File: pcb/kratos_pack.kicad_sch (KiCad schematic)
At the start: 97 parts, among them J1 USB_C_Receptacle_USB2.0, J2 PROG_CONN, J3 DBG_UART, J4 BAT_MID+NTC, J5 BAT_7.4V, J6 BAT_0V, J7 OUT+, J8 OUT-, Q1 AON7403, Q2 AON7414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

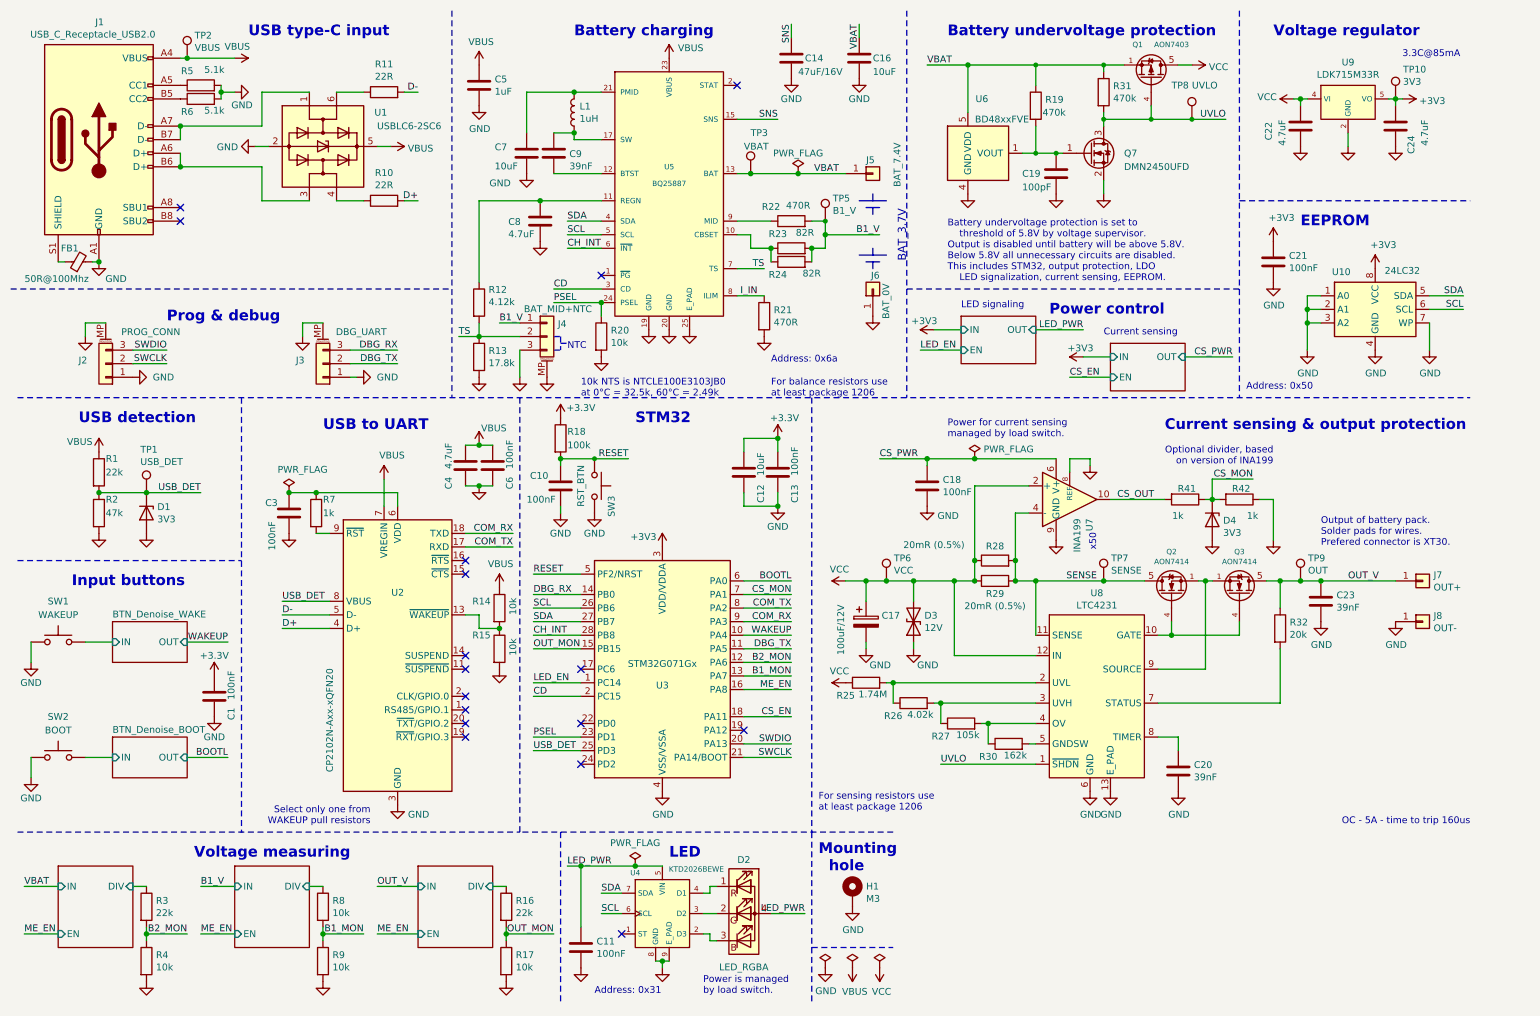
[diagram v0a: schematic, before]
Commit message: Schema & PCB: Fix USB detection by MCU and USB converter, hide GND labels
USB detection circuit is now connected only to MCU.
Converter from USB to UART (CP2102) is directly connected to VBUS.
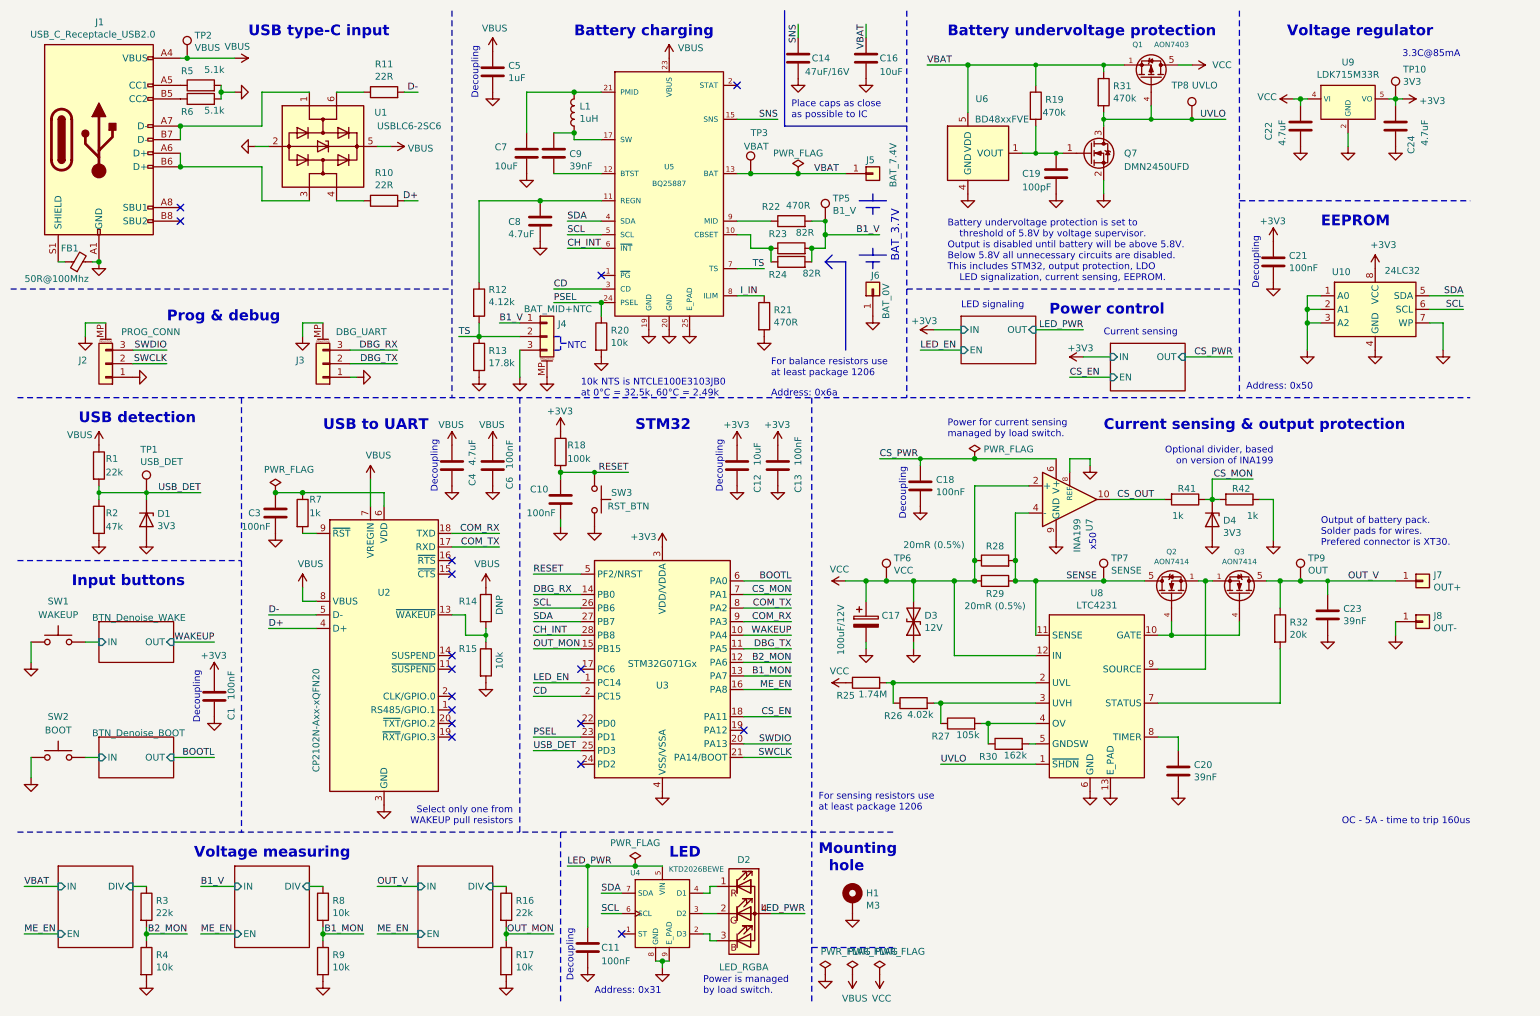
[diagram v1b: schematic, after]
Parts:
- R14: value 10k -> DNP
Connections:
- net USB_DET: no longer U2.8 (VBUS)
- net VBUS: now also U2.8 (VBUS)
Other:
- note added: "Decoupling"
- note added: "Place caps as close as possible to IC"
- moved on the sheet: C10, C11, C12, C13, C14, C16, C18, C23, C3, C4, C5, D1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

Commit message: Schema: Removed intended ILIM connection, mirror connectors, fix typos
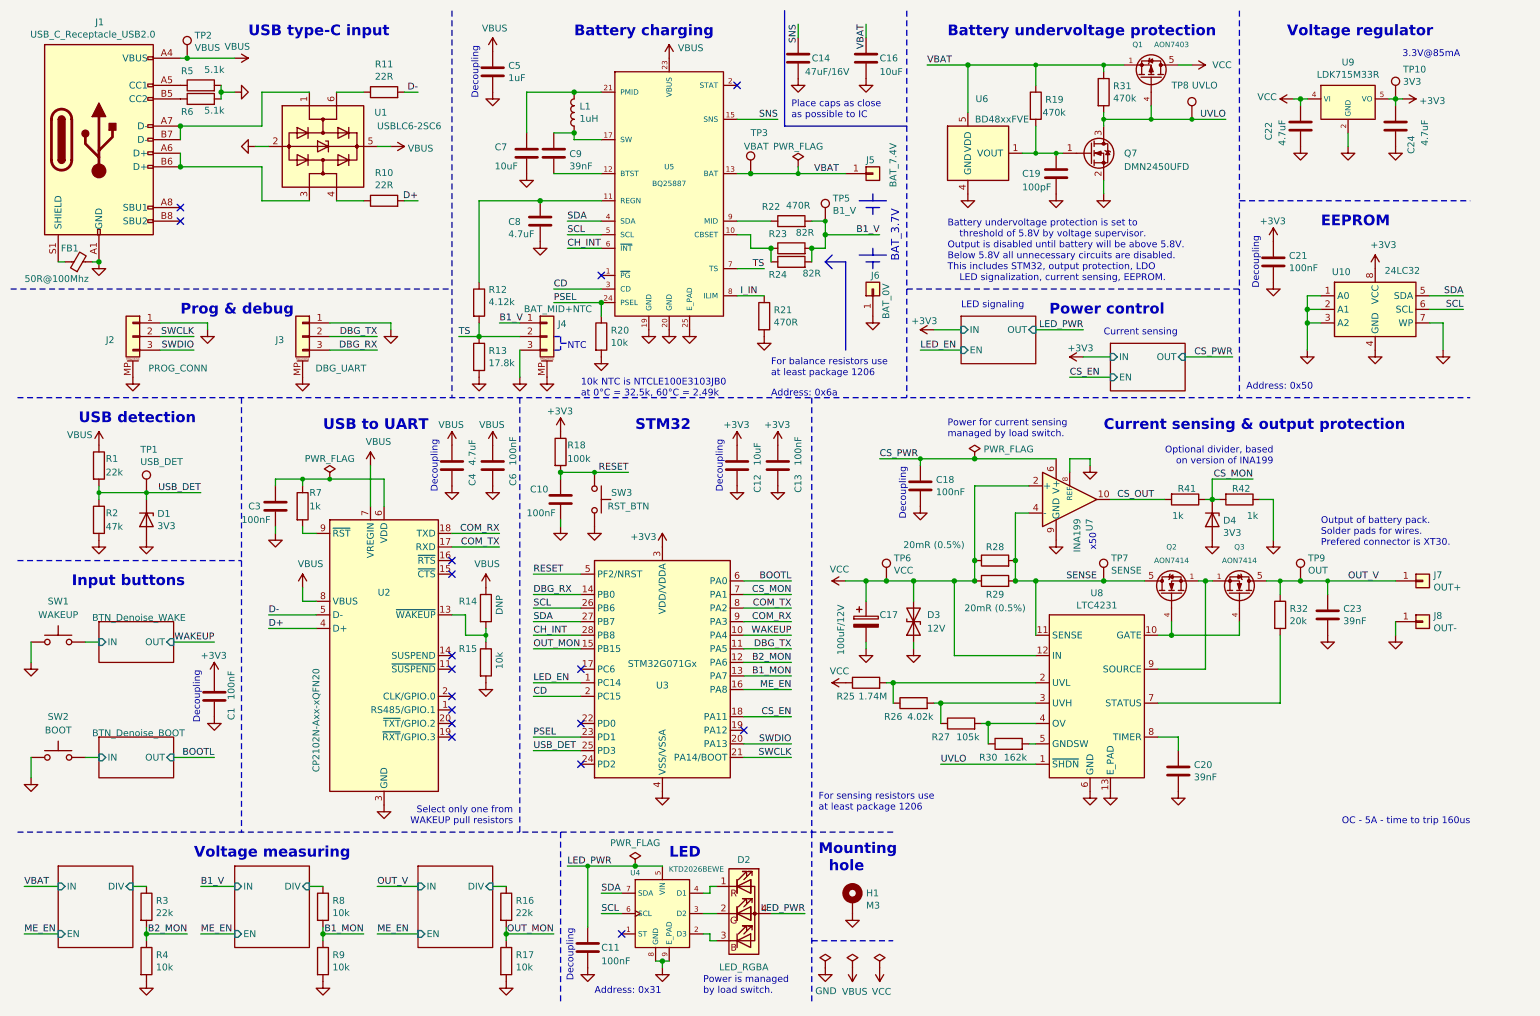
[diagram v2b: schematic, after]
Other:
- note added: "10k NTC is NTCLE100E3103JB0 at 0°C = 32.5k, 60°C = 2.49k"
- note added: "3.3V@85mA"
- note removed: "10k NTS is NTCLE100E3103JB0 at 0°C = 32.5k, 60°C = 2.49k"
- note removed: "3.3C@85mA"
- moved on the sheet: C3, J2, J3, R32, R7

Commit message: PCB: Fix footprint of signalization LED
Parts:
- D2: footprint Resistor_SMD:R_Array_Convex_2x0606 -> TCY_smd_leds:WL-SFCD - RGB606
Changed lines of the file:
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@@
     (property "Reference" "D2" (id 0) (at 148.59 171.5578 0))
     (property "Value" "LED_RGBA" (id 1) (at 148.59 191.6365 0))
-    (property "Footprint" "Resistor_SMD:R_Array_Convex_2x0606" (id 2) (at 148.59 182.88 0)
+    (property "Footprint" "TCY_smd_leds:WL-SFCD - RGB606" (id 2) (at 148.59 182.88 0)
       (effects (font (size 1.27 1.27)) hide)
     )
@@
     )
     (path "/59875fa1-96e8-4321-9ea5-fbd642347403"
-      (reference "D2") (unit 1) (value "LED_RGBA") (footprint "Resistor_SMD:R_Array_Convex_2x0606")
+      (reference "D2") (unit 1) (value "LED_RGBA") (footprint "TCY_smd_leds:WL-SFCD - RGB606")
     )
     (path "/00db56a2-afd7-45ee-a1df-242f89ea2fec"

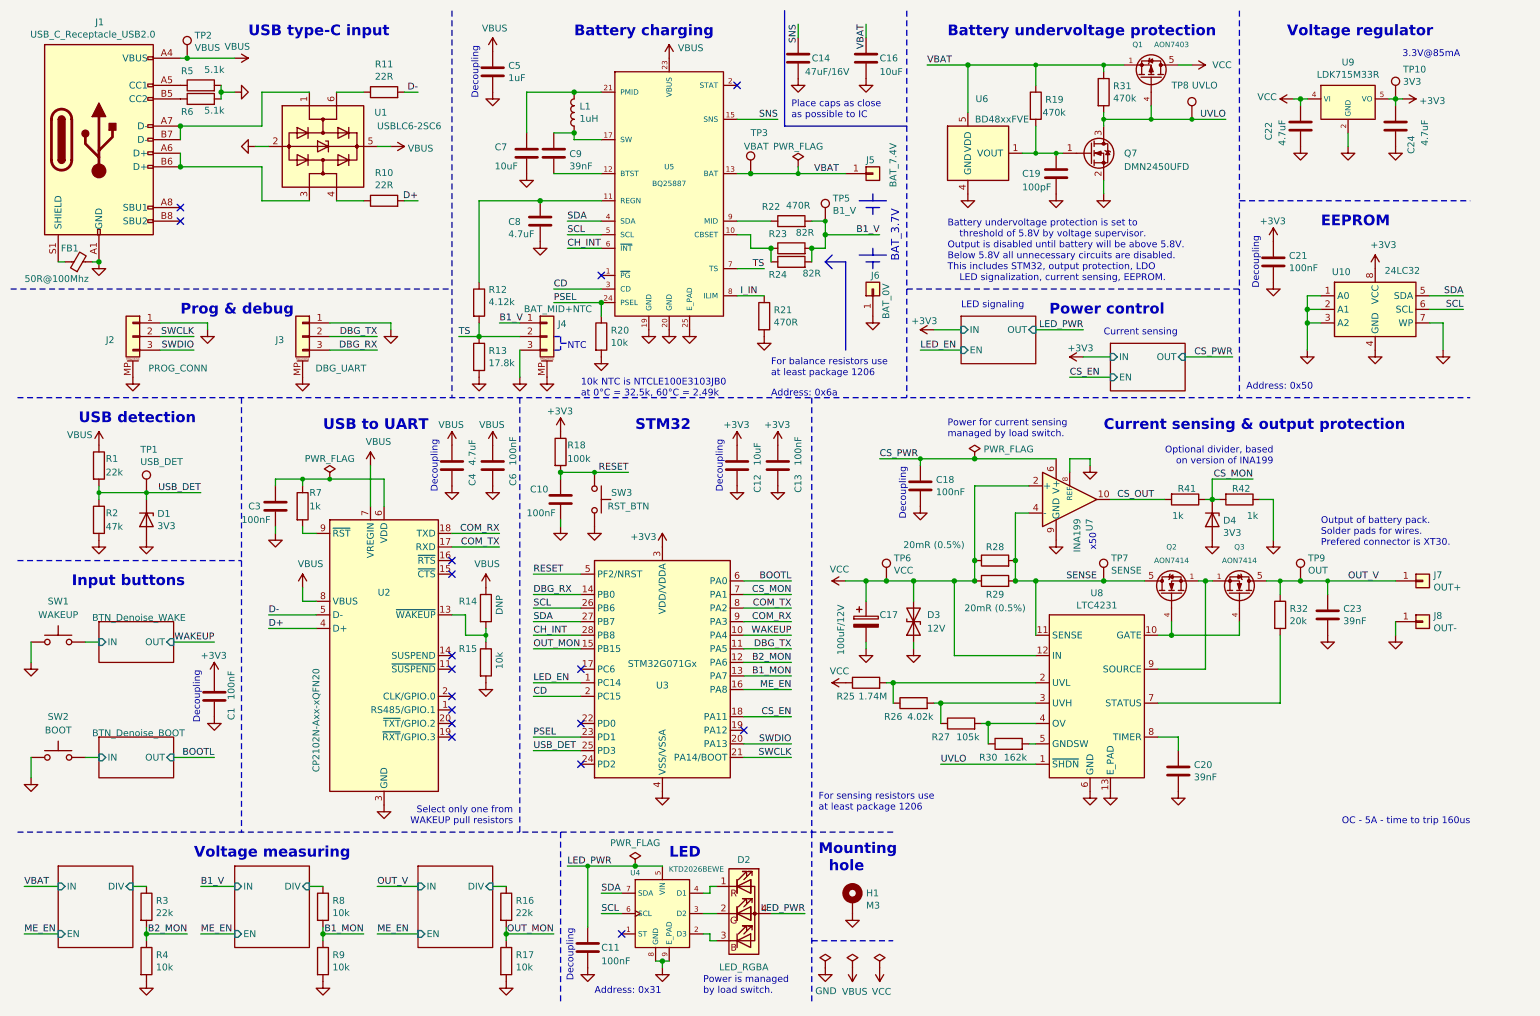
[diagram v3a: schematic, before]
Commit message: Schema: fix USB connection
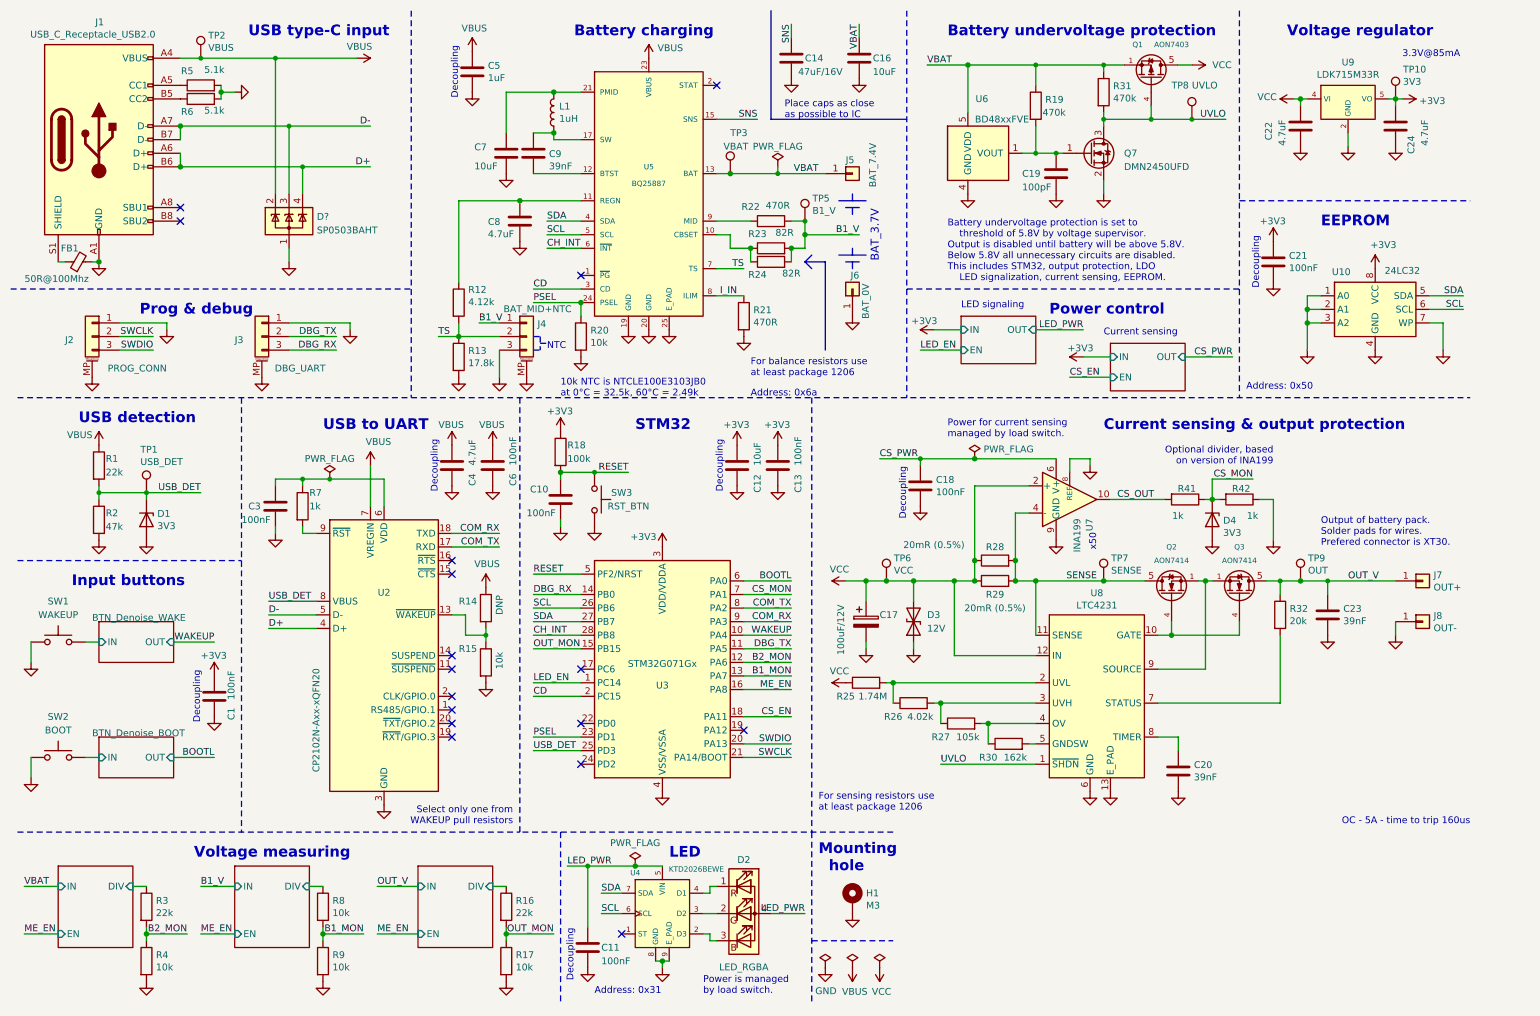
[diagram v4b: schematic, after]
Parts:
- removed R10, R11: 22R, TCY_passives:R_0603_1608Metric, symbol Device:R
- removed U1: USBLC6-2SC6, Package_TO_SOT_SMD:SOT-23-6, symbol Power_Protection:USBLC6-2SC6
- added D?: SP0503BAHT, Package_TO_SOT_SMD:SOT-143, symbol Power_Protection:SP0503BAHT
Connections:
- net D+: now also J1.A6 (D+), J1.B6 (D+), D?.4 (K)
- net D-: now also J1.A7 (D-), J1.B7 (D-), D?.3 (K)
- net GND: now also D?.1 (A)
- net USB_DET: now also U2.8 (VBUS)
- net VBUS: now also D?.2 (K); no longer U2.8 (VBUS)
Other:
- moved on the sheet: C14, C16, C5, C7, C8, C9, J2, J3, J4, J5, J6, L1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

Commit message: Schema & PCB: connect LTC4231 Shutdown pin to MCU GPIO
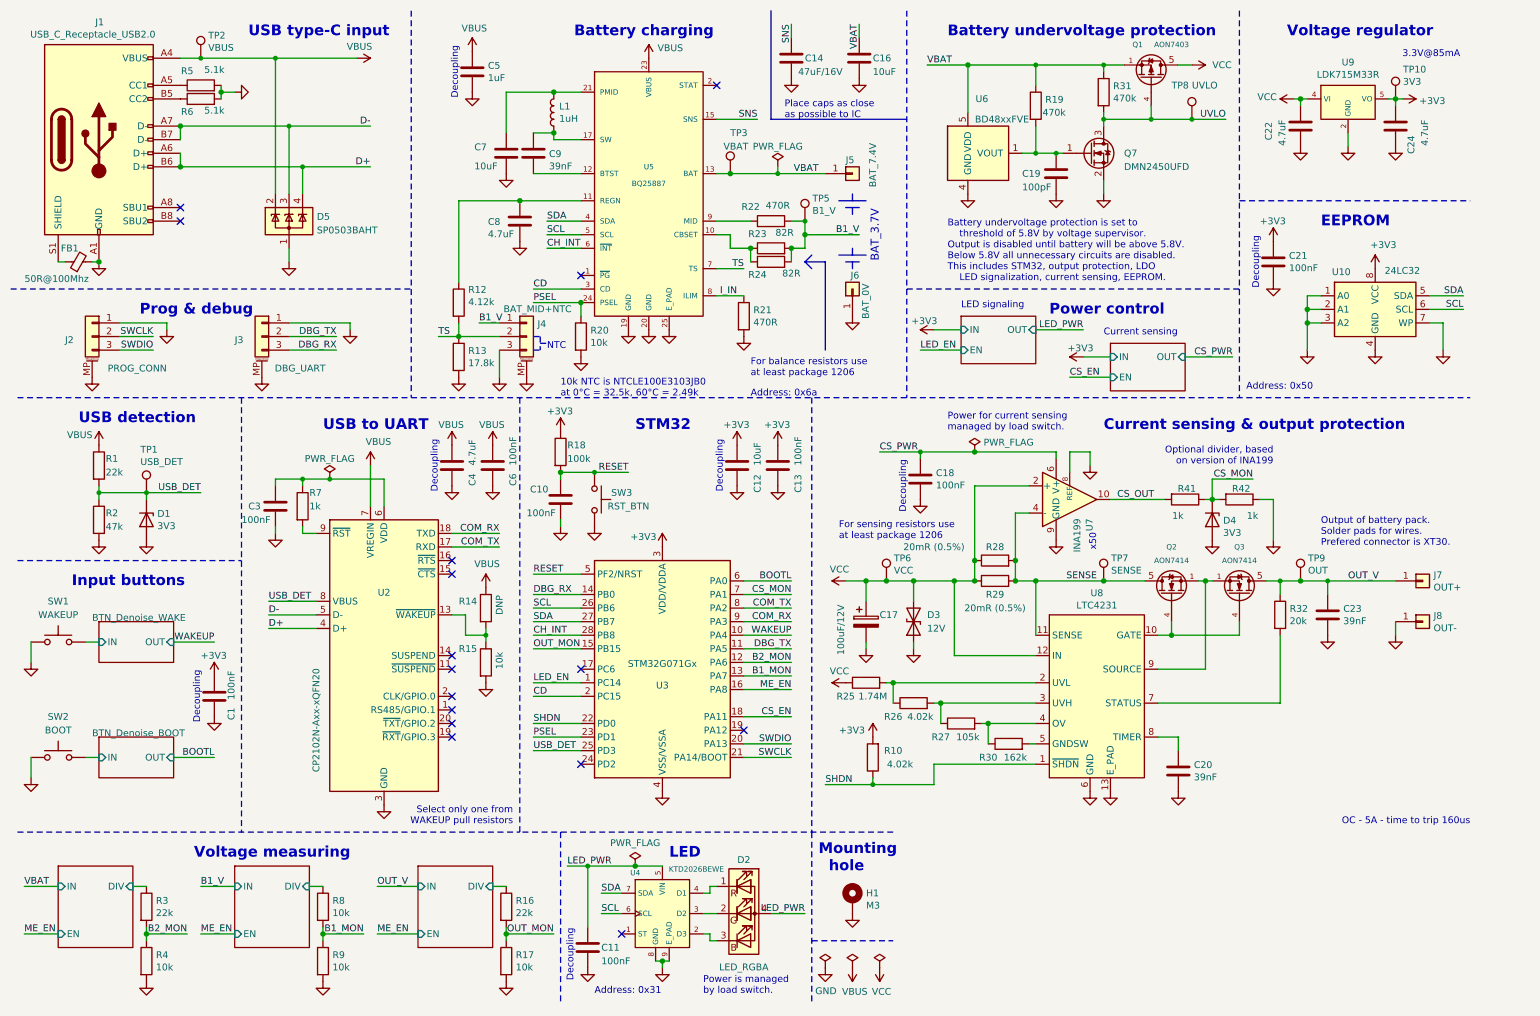
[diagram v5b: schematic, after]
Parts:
- added R10: 4.02k, TCY_passives:R_0603_1608Metric, symbol Device:R
- gave numbers to parts that had none: 1
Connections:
- net +3V3: now also R10.2
- net UVLO: no longer U8.1 (~{SHDN})
- net SHDN: now reaches U3.22 (PD0)
- net SHDN: now also U8.1 (~{SHDN}), R10.1
- no-connect marks 17 -> 16
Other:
- moved on the sheet: C18
